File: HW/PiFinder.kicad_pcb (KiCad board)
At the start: 2 copper layers, 16 x 14.5 mm, 12 parts, among them P1 CONN_01X05, U1 VL53L0X

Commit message: Finalized the design. Ready to order.
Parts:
- added REF**: via_0.3mm, KicadLibrary:via_0.3mm, F.Cu at (152.0, 100.5)
- U1: footprint KicadLibrary:VL53L0x -> KicadFootprint:VL53L0x
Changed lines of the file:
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@@
 (kicad_pcb (version 4) (host pcbnew 4.0.4-stable)
   (general
-    (links 26)
+    (links 27)
     (no_connects 0)
     (area 139.07381 97.845 159.533334 114.095001)
@@
     (tracks 82)
     (zones 0)
-    (modules 12)
+    (modules 13)
     (nets 8)
   )
@@
     (add_net "Net-(R4-Pad1)")
     (add_net "Net-(U1-Pad8)")
+    (add_net "Net-(U2-Pad1)")
+    (add_net "Net-(U2-Pad10)")
+    (add_net "Net-(U2-Pad11)")
+    (add_net "Net-(U2-Pad12)")
+    (add_net "Net-(U2-Pad2)")
+    (add_net "Net-(U2-Pad3)")
+    (add_net "Net-(U2-Pad4)")
+    (add_net "Net-(U2-Pad5)")
+    (add_net "Net-(U2-Pad6)")
+    (add_net "Net-(U2-Pad7)")
+    (add_net "Net-(U2-Pad8)")
+    (add_net "Net-(U2-Pad9)")
     (add_net VCC)
+  )
+  (module KicadLibrary:via_0.3mm (layer F.Cu)
+    (at 152 100.5)
+    (fp_text reference REF** (at 0 1.27) (layer F.SilkS) hide
+      (effects (font (size 1 1) (thickness 0.15)))
+    )
+    (fp_text value via_0.3mm (at 0 -1.27) (layer F.Fab) hide
+      (effects (font (size 1 1) (thickness 0.15)))
+    )
+    (pad 1 thru_hole circle (at 0 0) (size 0.6 0.6) (drill 0.3) (layers *.Cu)
+      (net 1 GND) (zone_connect 2))
   )
   (module KicadLibrary:via_0.3mm (layer F.Cu)
@@
     (descr "Through hole pin header")
     (tags "pin header")
-    (fp_text reference P1 (at -2.5 5.58) (layer F.SilkS)
+    (fp_text reference P1 (at -2.5 3.08) (layer F.SilkS)
       (effects (font (size 1 1) (thickness 0.15)))
     )
@@
     )
   )
-  (module KicadLibrary:VL53L0x (layer F.Cu)
+  (module KicadFootprint:VL53L0x (layer F.Cu)
     (at 148.5 107 90)
-    (fp_text reference U1 (at 3 -0.25 180) (layer F.SilkS)
-      (effects (font (size 1 1) (thickness 0.15)))
-    )
-    (fp_text value VL53L0X (at -2 3.75 180) (layer F.Fab) hide
-      (effects (font (size 1 1) (thickness 0.15)))
-    )
+    (fp_text reference U1 (at -0.25 2.5 180) (layer F.SilkS)
+      (effects (font (size 1 1) (thickness 0.15)))
+    )
+    (fp_text value VL53L0X (at 0 -2.8 90) (layer F.Fab)
+      (effects (font (size 1 1) (thickness 0.15)))
+    )
+    (fp_line (start -2.2 1.2) (end -2.2 -1.2) (layer F.SilkS) (width 0.25))
+    (fp_line (start 2.2 1.2) (end -2.2 1.2) (layer F.SilkS) (width 0.25))
+    (fp_line (start 2.2 -1.2) (end 2.2 1.2) (layer F.SilkS) (width 0.25))
+    (fp_line (start -2.2 -1.2) (end 2.2 -1.2) (layer F.SilkS) (width 0.25))
     (fp_circle (center -2.9 -1.5) (end -2.8 -1.3) (layer F.SilkS) (width 0.15))
     (pad 1 smd rect (at -1.65 -0.85 90) (size 0.5 0.5) (layers F.Cu F.Paste F.Mask)

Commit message: Order the PCB.
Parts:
- added G***: LOGO, KicadFootprint:LOGO, B.Cu at (146.8, 108.4)
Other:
- board text added: "PiFinder Rev A qnibbles LLC Copyright 2016"
- board text removed: "PiFinder V1 Blackbird Engineering"

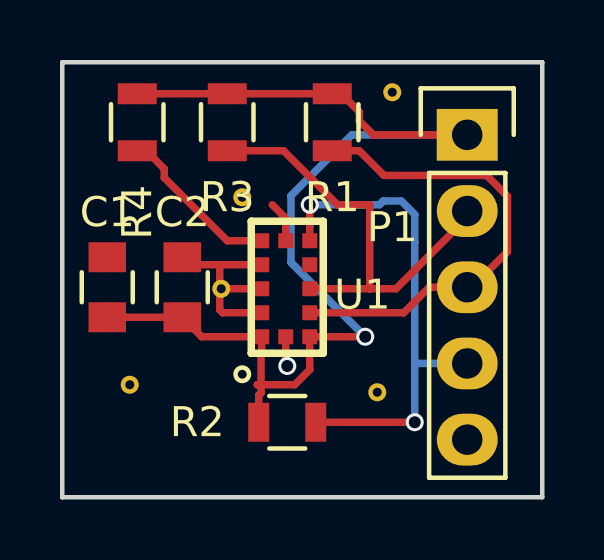
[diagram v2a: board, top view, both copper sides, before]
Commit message: Updated some of the silk screen.
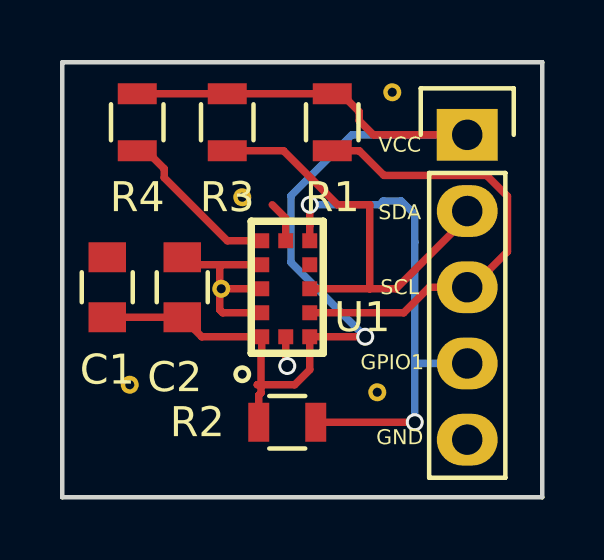
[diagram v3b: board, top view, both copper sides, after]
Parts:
- removed G***: LOGO, KicadFootprint:LOGO
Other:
- board text added: "GND"
- board text added: "GPIO1"
- board text added: "PiFinder Rev A QNibbles LLC Copyright 2017"
- board text added: "SCL"
- board text added: "SDA"
- board text added: "VCC"
- board text removed: "PiFinder Rev A qnibbles LLC Copyright 2016"
